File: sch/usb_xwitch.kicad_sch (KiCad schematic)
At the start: 71 parts, among them J1 USB3_A, J2 USB3_A, J3 USB3_A, J5 USB3_A, J6 USB3_A, J7 USB3_A, J8 Conn_02x05_Odd_Even, J9 C65114, K1 Relay_DPDT_Panasonic_AGQ200A4H, K2 Relay_DPDT_Panasonic_AGQ200A4H, K3 Relay_DPDT_Panasonic_AGQ200A4H, Q1 2N7002P, Q2 2N7002P, Q3 2N7002P, SW1 C2689642, U1 Pico

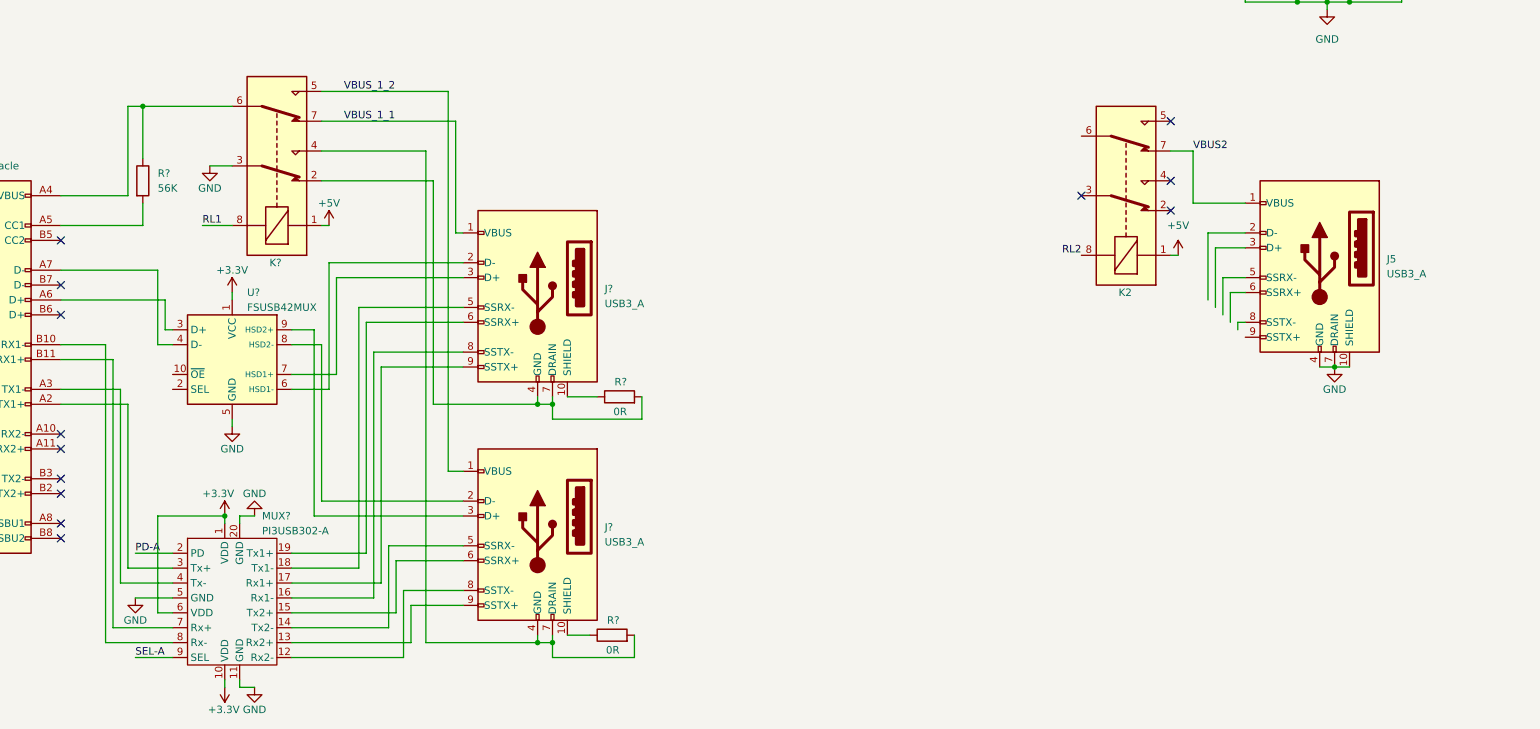
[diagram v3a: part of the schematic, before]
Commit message: updated usbc schematics
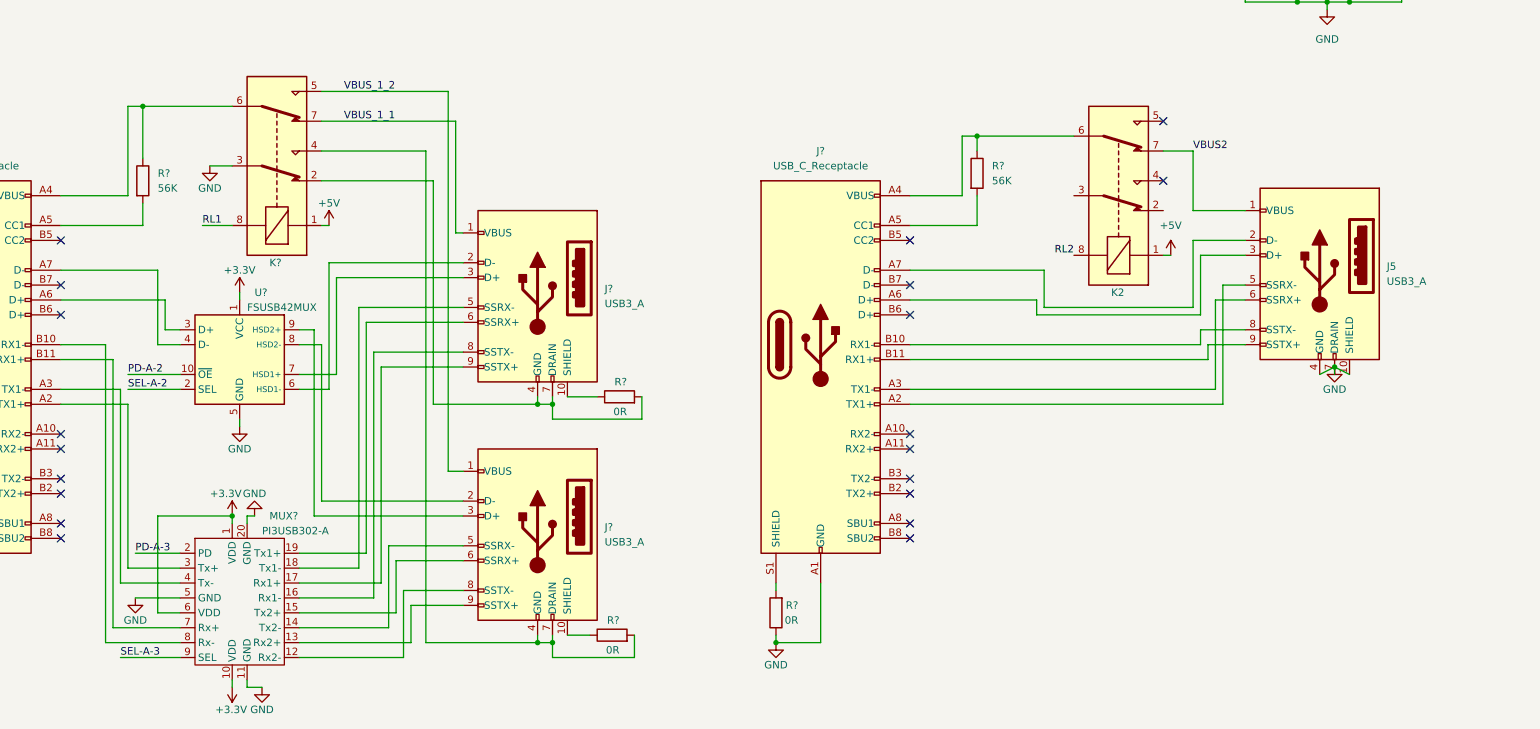
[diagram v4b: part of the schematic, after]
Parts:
- added J?: USB_C_Receptacle, usb_xwitch:USB_TypeC_24Pin_ShouHan, symbol Connector:USB_C_Receptacle
- added R?: 56K, Resistor_SMD:R_0402_1005Metric_Pad0.72x0.64mm_HandSolder, symbol Device:R
- added R?: 0R, Resistor_SMD:R_0603_1608Metric_Pad0.98x0.95mm_HandSolder, symbol Device:R
- J?: LCSC (none) -> C456013
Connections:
- net GND: now also J?.A1 (GND), J?.A12 (GND), J?.B1 (GND), J?.B12 (GND), R?.1
- net PD-A: no longer MUX?.2 (PD)
- net SEL-A: no longer MUX?.9 (SEL)
- net PD-A-2: now reaches U?.10 (~{OE})
- net SEL-A-2: now reaches U?.2 (SEL)
- net at K2.6: now also J?.A4 (VBUS), J?.A9 (VBUS), J?.B4 (VBUS), J?.B9 (VBUS), R?.1
- net at J5.2 (D-): now also J?.A7 (D-)
- net at J5.3 (D+): now also J?.A6 (D+)
- net at J5.5 (SSRX-): now also J?.A2 (TX1+)
- net at J5.6 (SSRX+): now also J?.A3 (TX1-)
- net at J5.8 (SSTX-): now also J?.B10 (RX1-)
- net at J5.9 (SSTX+): now also J?.B11 (RX1+)
- new net: J?.A5 (CC1), R?.2
- new net: J?.S1 (SHIELD), R?.2
- new net PD-A-3: MUX?.2 (PD)
- new net SEL-A-3: MUX?.9 (SEL)
- no-connect marks 46 -> 53
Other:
- moved on the sheet: J5, K2, MUX?, U?

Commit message: more  usb-c channels update
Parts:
- removed C1, C2, C3, C4, C5, C6, C7, C8: 100n, Capacitor_SMD:C_0805_2012Metric_Pad1.18x1.45mm_HandSolder, symbol Device:C
- removed J1, J2, J3, J6: USB3_A, usb_xwitch:USB3_A_AdamTech_USB-A3-S-RA, symbol Connector:USB3_A
- removed JP1, JP2, JP3, JP4: SolderJumper_2_Open, Jumper:SolderJumper-2_P1.3mm_Open_RoundedPad1.0x1.5mm, symbol Jumper:SolderJumper_2_Open
- removed K1, K3: Relay_DPDT_Panasonic_AGQ200A4H, usb_xwitch:Relay_DPDT_Panasonic_AGQ200A4H, symbol usb_xwitch:Relay_DPDT_Panasonic_AGQ200A4H
- removed MUX1: PI3USB302-A, usb_xwitch:USB_MUX_DEMUX_PI3USB302-A, symbol usb_xwitch:PI3USB302-A
- added J6: USB_C_Receptacle, usb_xwitch:USB_TypeC_24Pin_ShouHan, symbol Connector:USB_C_Receptacle
- added K?: Relay_DPDT_Panasonic_AGQ200A4H, usb_xwitch:Relay_DPDT_Panasonic_AGQ200A4H, symbol usb_xwitch:Relay_DPDT_Panasonic_AGQ200A4H
- added R? (x7): 0R, Resistor_SMD:R_0603_1608Metric_Pad0.98x0.95mm_HandSolder, symbol Device:R
- added R?: 56K, Resistor_SMD:R_0402_1005Metric_Pad0.72x0.64mm_HandSolder, symbol Device:R
- J5, J7: LCSC (none) -> C69073
- gave numbers to parts that had none: 1
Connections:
- net +5V: now also K?.1
- net GND: now also K2.3, J6.A1 (GND), J6.A12 (GND), J6.B1 (GND), J6.B12 (GND), K?.3, R?.1, R?.2, R?.2, R?.2, R?.2; no longer J5.10 (SHIELD), J5.4 (GND), J5.7 (DRAIN), J7.10 (SHIELD), J7.4 (GND), J7.7 (DRAIN)
- net RL3: now also K?.8
- net VBUS3: now also K?.7
- net at K2.2: now also J5.4 (GND), J5.7 (DRAIN), R?.1, R?.2
- net at J?.4 (GND), J?.7 (DRAIN), K?.2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: now also R?.1
- net at J?.4 (GND), J?.7 (DRAIN), K?.4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: now also R?.1
- net at J5.5 (SSRX-): now also J4.A3 (TX1-); no longer J4.A2 (TX1+)
- net at J5.6 (SSRX+): now also J4.A2 (TX1+); no longer J4.A3 (TX1-)
- net at J7.2 (D-): now also J6.A7 (D-)
- net at J7.3 (D+): now also J6.A6 (D+)
- net at J7.5 (SSRX-): now also J6.A3 (TX1-)
- net at J7.6 (SSRX+): now also J6.A2 (TX1+)
- net at J7.8 (SSTX-): now also J6.B10 (RX1-)
- net at J7.9 (SSTX+): now also J6.B11 (RX1+)
- new net: J5.10 (SHIELD), R?.1
- new net: J6.S1 (SHIELD), R?.2
- new net: J7.4 (GND), J7.7 (DRAIN), K?.2, R?.1, R?.2
- new net: J6.A4 (VBUS), J6.A9 (VBUS), J6.B4 (VBUS), J6.B9 (VBUS), K?.6, R?.1
- new net: J6.A5 (CC1), R?.2
- new net: J7.10 (SHIELD), R?.1
- no-connect marks 53 -> 57
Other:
- sheet xwitch_controller ports: added GPIO0; removed none
- moved on the sheet: C9, D2, D3, D4, D5, D6, D7, D8, D?, J4, J5, J8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

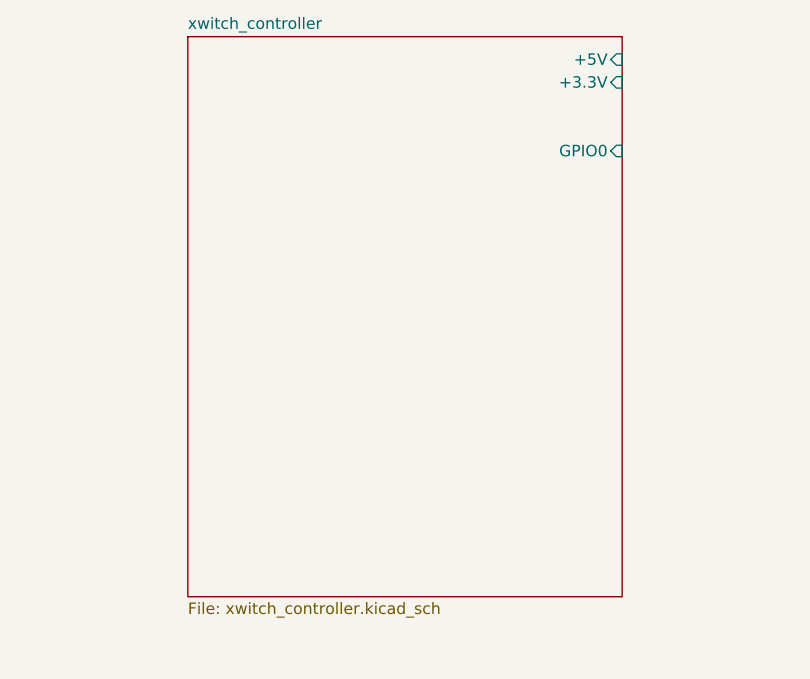
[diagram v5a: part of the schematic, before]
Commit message: updated pico pinout
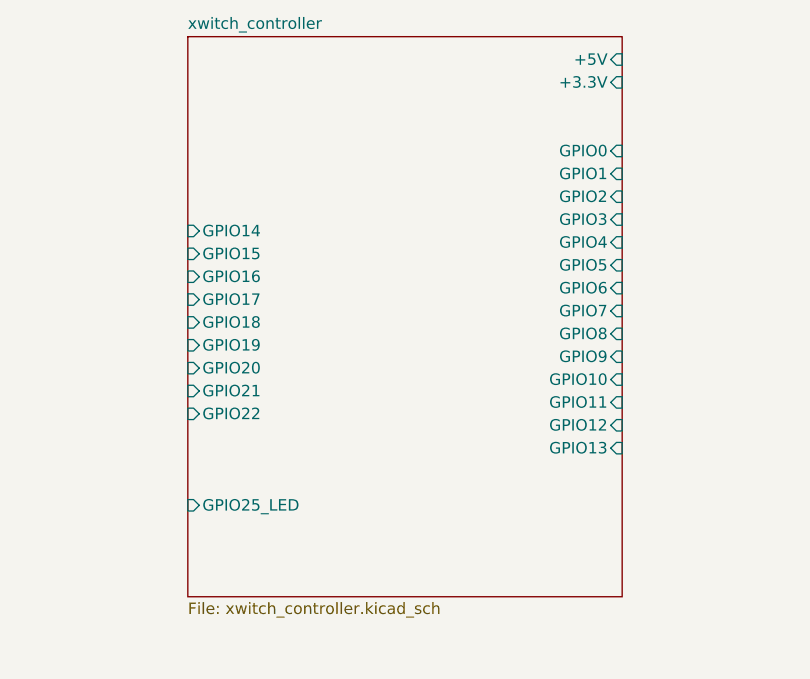
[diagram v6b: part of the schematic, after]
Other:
- sheet xwitch_controller ports: added GPIO1, GPIO10, GPIO11, GPIO12, GPIO13, GPIO14, GPIO15, GPIO16, GPIO17, GPIO18, GPIO19, GPIO2, GPIO20, GPIO21, GPIO22, GPIO25_LED, GPIO3, GPIO4, GPIO5, GPIO6, GPIO7, GPIO8, GPIO9; removed none
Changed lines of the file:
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@@
+      (effects (font (size 1.27 1.27)) (justify right))
+    )
+    (pin "GPIO1" input (at 88.9 111.76 0)
+      (effects (font (size 1.27 1.27)) (justify right))
+    )
+    (pin "GPIO21" input (at 40.64 135.89 180)
+      (effects (font (size 1.27 1.27)) (justify left))
+    )
+    (pin "GPIO25_LED" input (at 40.64 148.59 180)
+      (effects (font (size 1.27 1.27)) (justify left))
+    )
+    (pin "GPIO22" input (at 40.64 138.43 180)
+      (effects (font (size 1.27 1.27)) (justify left))
+    )
+    (pin "GPIO20" input (at 40.64 133.35 180)
+      (effects (font (size 1.27 1.27)) (justify left))
+    )
+    (pin "GPIO17" input (at 40.64 125.73 180)
+      (effects (font (size 1.27 1.27)) (justify left))
+    )
+    (pin "GPIO14" input (at 40.64 118.11 180)
+      (effects (font (size 1.27 1.27)) (justify left))
+    )
+    (pin "GPIO19" input (at 40.64 130.81 180)
+      (effects (font (size 1.27 1.27)) (justify left))
+    )
+    (pin "GPIO16" input (at 40.64 123.19 180)
+      (effects (font (size 1.27 1.27)) (justify left))
+    )
+    (pin "GPIO18" input (at 40.64 128.27 180)
+      (effects (font (size 1.27 1.27)) (justify left))
+    )
+    (pin "GPIO15" input (at 40.64 120.65 180)
+      (effects (font (size 1.27 1.27)) (justify left))
+    )
+    (pin "GPIO2" input (at 88.9 114.3 0)
+      (effects (font (size 1.27 1.27)) (justify right))
+    )
+    (pin "GPIO5" input (at 88.9 121.92 0)
+      (effects (font (size 1.27 1.27)) (justify right))
+    )
+    (pin "GPIO3" input (at 88.9 116.84 0)
+      (effects (font (size 1.27 1.27)) (justify right))
+    )
+    (pin "GPIO4" input (at 88.9 119.38 0)
+      (effects (font (size 1.27 1.27)) (justify right))
+    )
+    (pin "GPIO7" input (at 88.9 127 0)
+      (effects (font (size 1.27 1.27)) (justify right))
+    )
+    (pin "GPIO6" input (at 88.9 124.46 0)
+      (effects (font (size 1.27 1.27)) (justify right))
+    )
+    (pin "GPIO8" input (at 88.9 129.54 0)
+      (effects (font (size 1.27 1.27)) (justify right))
+    )
+    (pin "GPIO11" input (at 88.9 137.16 0)
+      (effects (font (size 1.27 1.27)) (justify right))
+    )
+    (pin "GPIO12" input (at 88.9 139.7 0)
+      (effects (font (size 1.27 1.27)) (justify right))
+    )
+    (pin "GPIO13" input (at 88.9 142.24 0)
+      (effects (font (size 1.27 1.27)) (justify right))
+    )
+    (pin "GPIO9" input (at 88.9 132.08 0)
+      (effects (font (size 1.27 1.27)) (justify right))
+    )
+    (pin "GPIO10" input (at 88.9 134.62 0)
       (effects (font (size 1.27 1.27)) (justify right))
     )

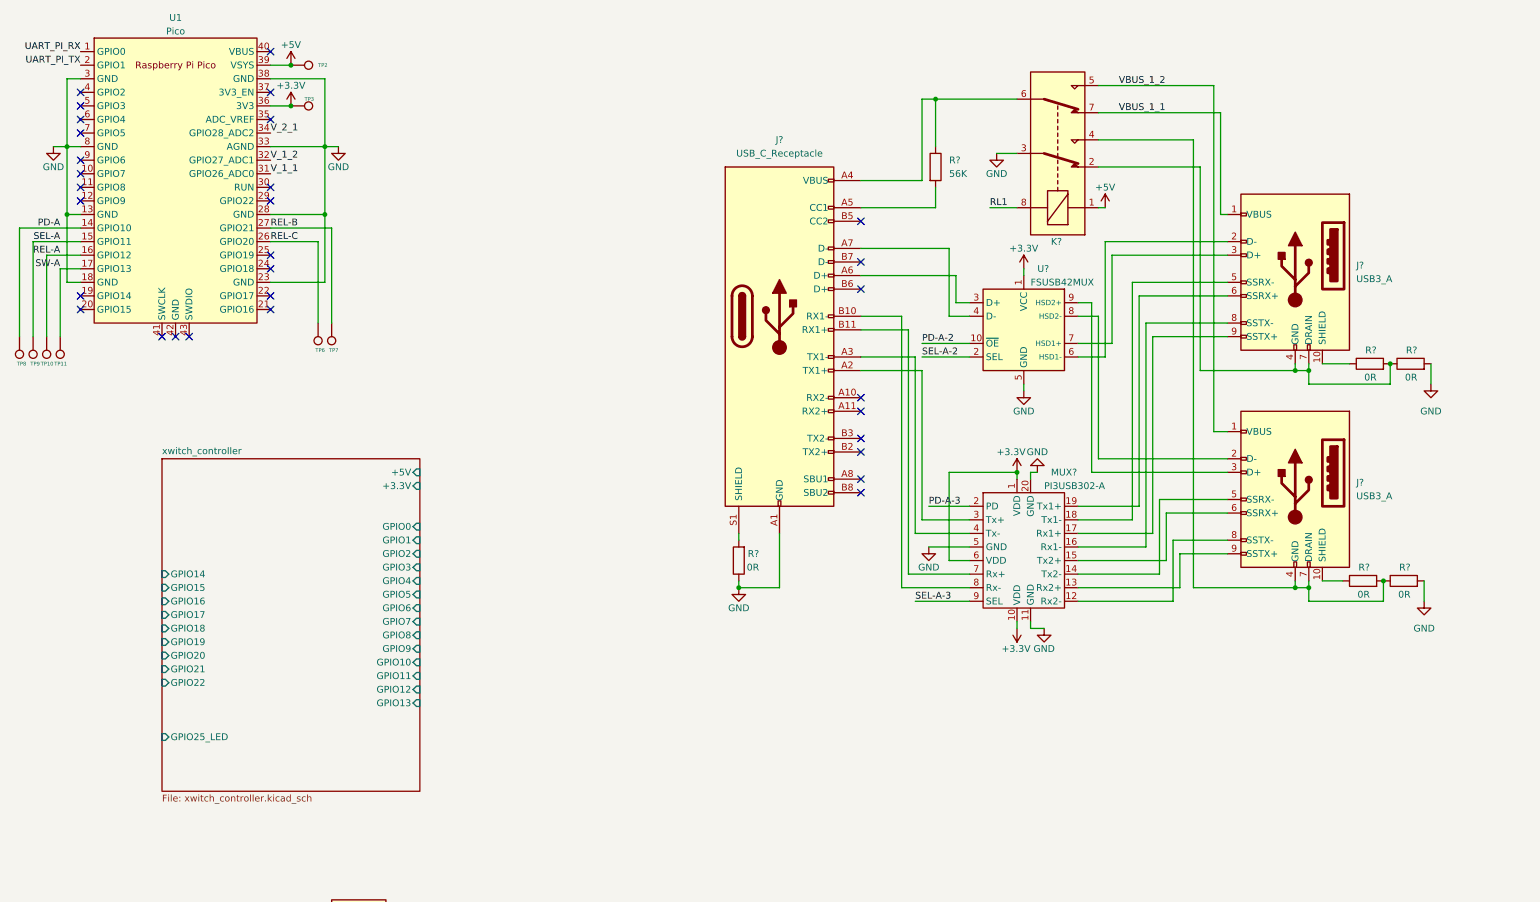
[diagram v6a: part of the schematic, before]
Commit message: replaced old pico board connection to embedded rp2040
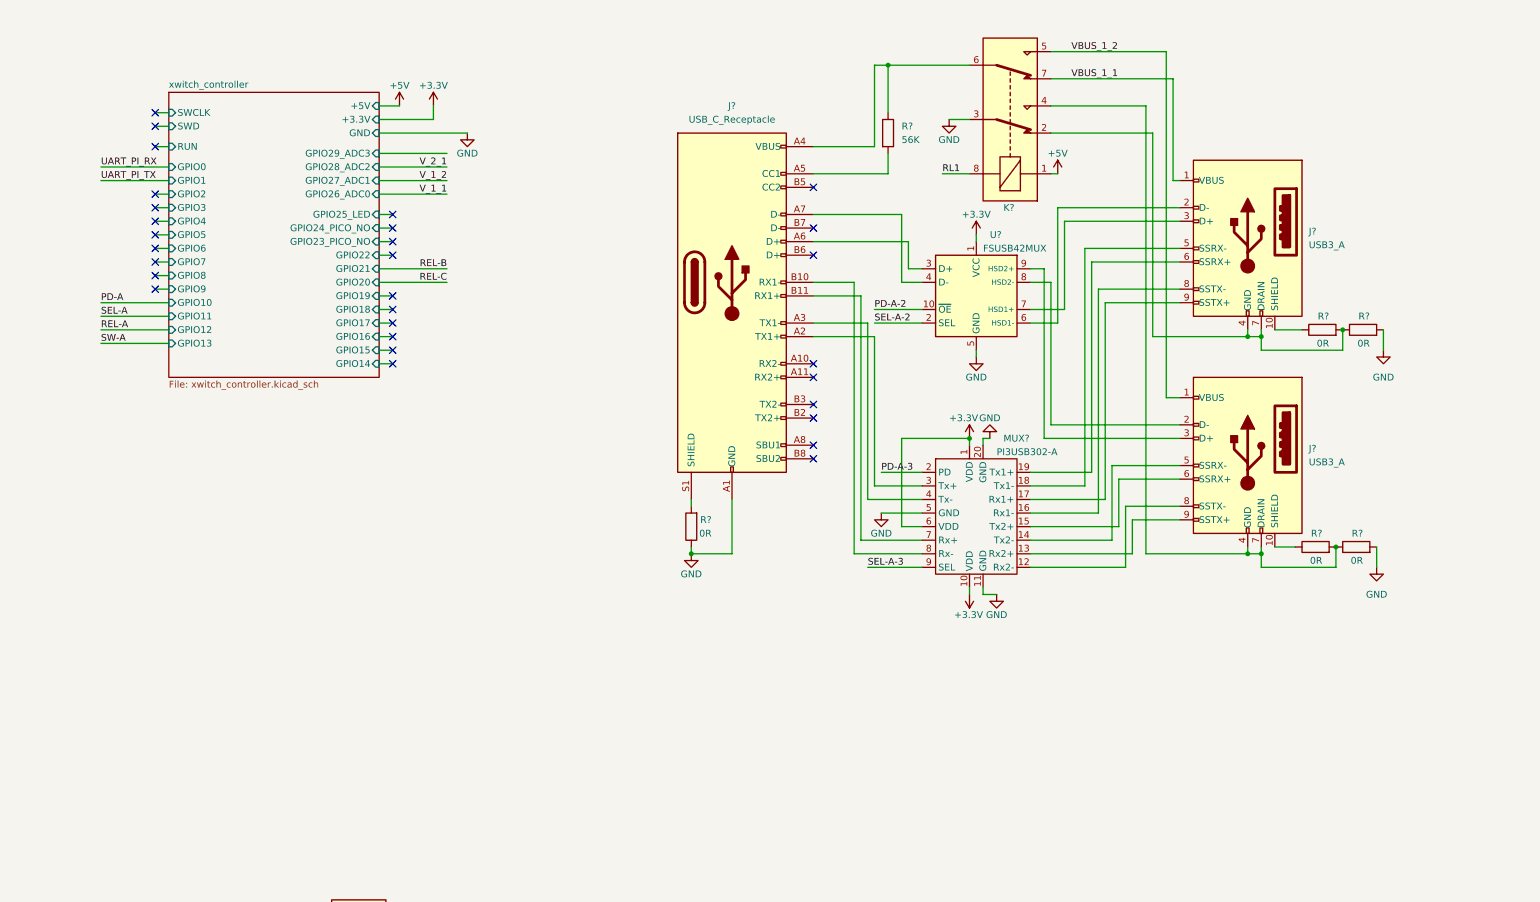
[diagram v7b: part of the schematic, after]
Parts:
- removed TP10, TP11, TP2, TP3, TP6, TP7, TP8, TP9: TestPoint, TestPoint:TestPoint_Pad_D1.0mm, symbol Connector:TestPoint
- removed U1: Pico, usb_xwitch:RPi_Pico_SMD, symbol usb_xwitch:Pico
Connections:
- no-connect marks 57 -> 56
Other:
- sheet xwitch_controller ports: added GND, GPIO23_PICO_NO, GPIO24_PICO_NO, GPIO26_ADC0, GPIO27_ADC1, GPIO28_ADC2, GPIO29_ADC3, RUN, SWCLK, SWD; removed none
- moved on the sheet: J?, K?, MUX?, R?, U?
